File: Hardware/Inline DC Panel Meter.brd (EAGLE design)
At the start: 73.7 x 40.6 mm, 36 parts, among them J1 POWER_JACKPOWER_JACK_SLOT

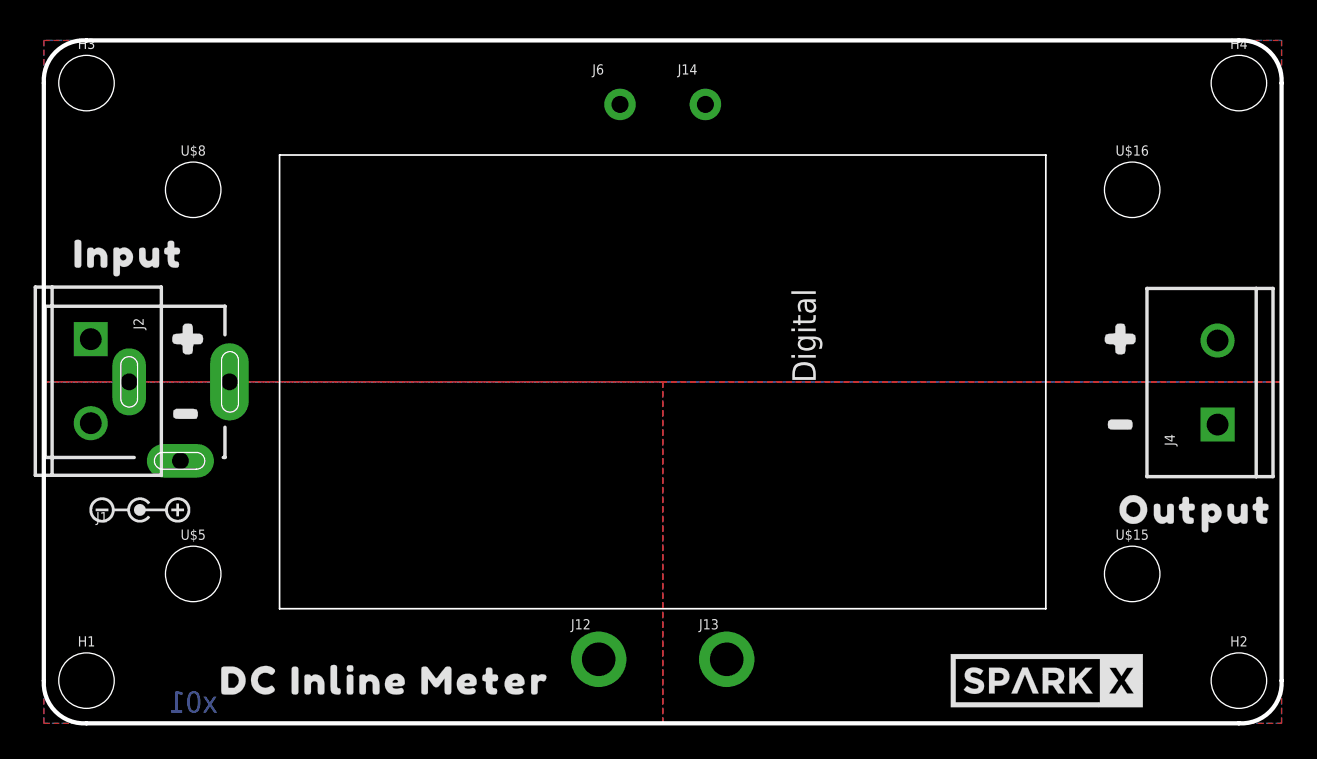
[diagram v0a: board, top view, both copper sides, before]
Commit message: Decrease window size for x02.
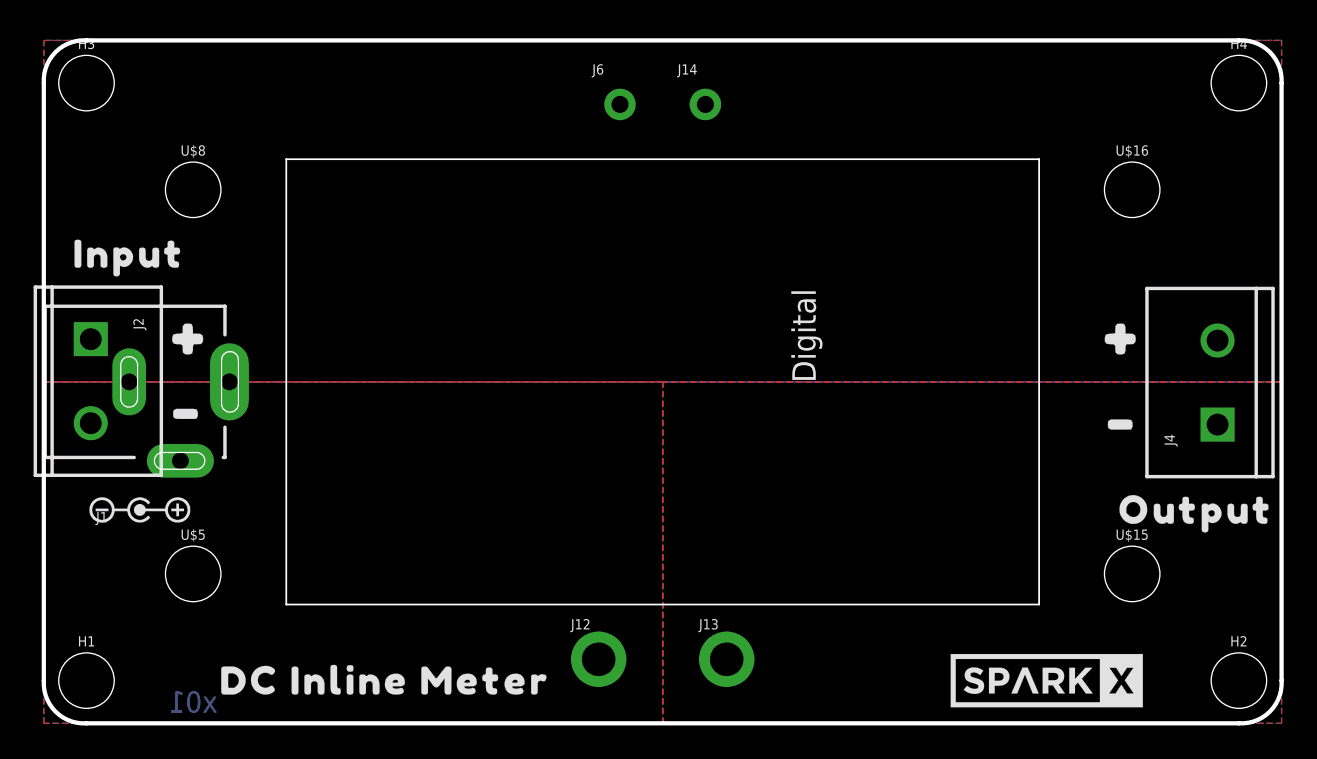
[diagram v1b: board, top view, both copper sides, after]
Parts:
- removed U$6: (no value), LFP-Battery-Bridge:METER
- added U$17: (no value), Panel Mount Meter:METER
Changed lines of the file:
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@@
 <layer number="47" name="Measures" color="7" fill="1" visible="no" active="yes"/>
 <layer number="48" name="Document" color="7" fill="1" visible="no" active="yes"/>
-<layer number="49" name="Reference" color="7" fill="1" visible="yes" active="yes"/>
+<layer number="49" name="Reference" color="7" fill="1" visible="no" active="yes"/>
 <layer number="50" name="dxf" color="7" fill="1" visible="no" active="yes"/>
 <layer number="51" name="tDocu" color="6" fill="1" visible="yes" active="yes"/>
@@
 </element>
 <element name="U$21" library="SparkX" package="SPARKX-LARGE" value="SPARKX-LOGO5" x="59.69" y="2.54" smashed="yes" rot="MR0"/>
-<element name="U$6" library="LFP-Battery-Bridge" package="METER" value="" x="36.83" y="20.32" smashed="yes"/>
 <element name="U$8" library="SparkFun-Hardware" package="STAND-OFF" value="" x="8.89" y="31.75" smashed="yes">
 <attribute name="NAME" x="8.89" y="33.782" size="0.6096" layer="25" font="vector" ratio="20" align="bottom-center"/>
@@
 <attribute name="REV" value="" x="0" y="-21.59" size="1.778" layer="27" font="vector" ratio="15" display="off"/>
 </element>
+<element name="U$17" library="Panel Mount Meter" package="METER" value="" x="36.83" y="20.32" smashed="yes"/>
 </elements>
 <signals>
